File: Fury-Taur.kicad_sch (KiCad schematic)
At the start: 25 parts, among them J1 Pickup, J2 Output, J3 Audio Out, Q1 J201, Q2 J201, SW1 SW_SPDT

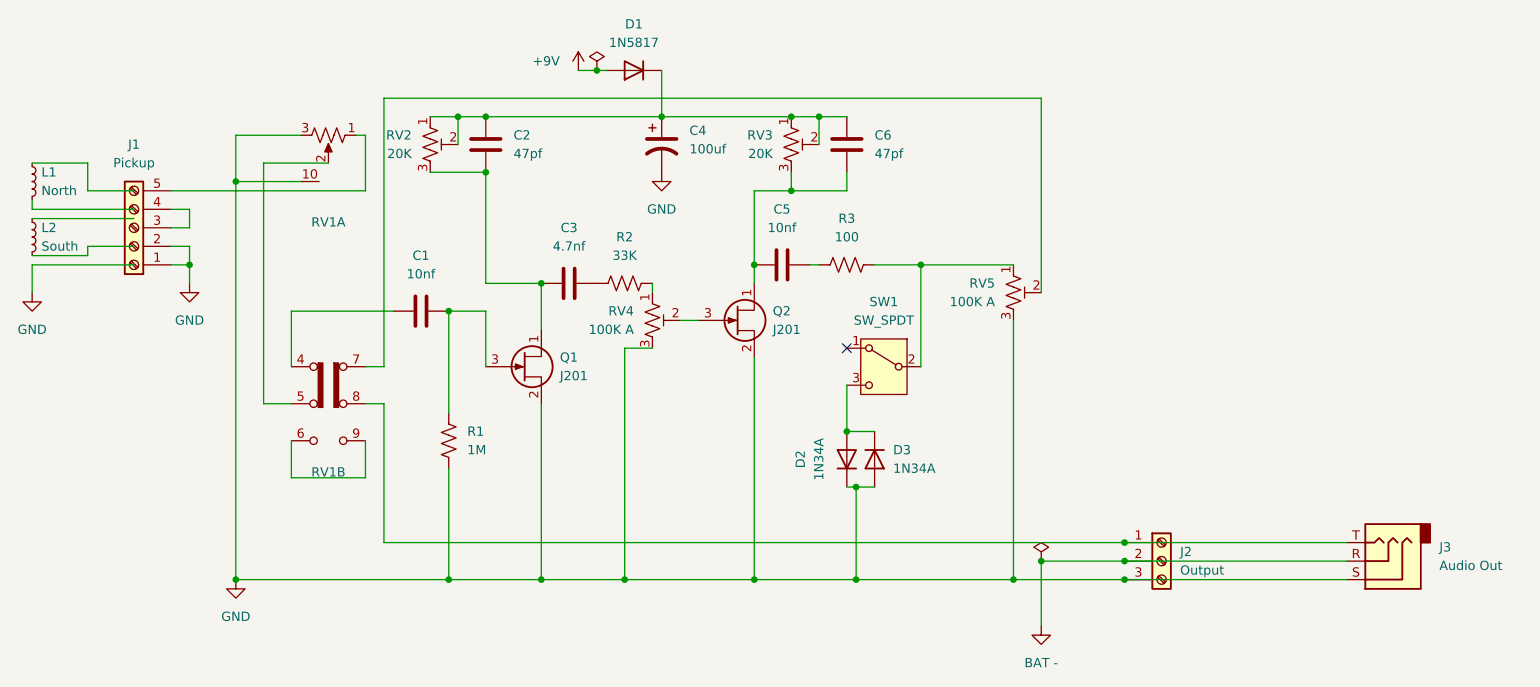
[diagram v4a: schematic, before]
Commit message: Added custom Humbucker symbol on Schematic
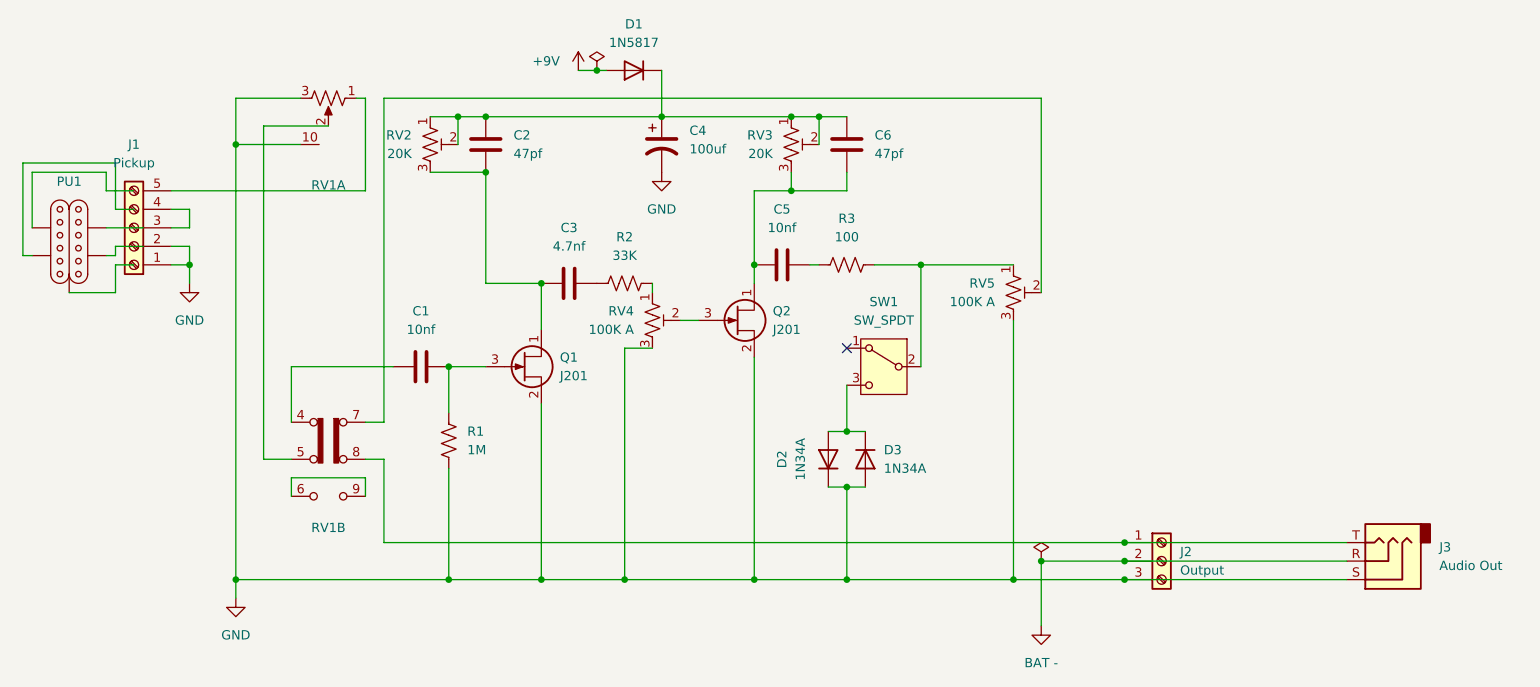
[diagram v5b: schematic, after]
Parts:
- removed L1: North, symbol Device:L_Small
- removed L2: South, symbol Device:L_Small
- added PU1: (no value), symbol CustomSymbols:Humbucker_4Cond_SD
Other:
- moved on the sheet: C1, D2, D3, RV1A, RV1B
